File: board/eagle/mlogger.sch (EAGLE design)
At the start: 40 parts, among them J1 MICROSD-9P, SW1 SS-12D00G3, SW2 TVAF06-A020B-R, SW3 TVAF06-A020B-R

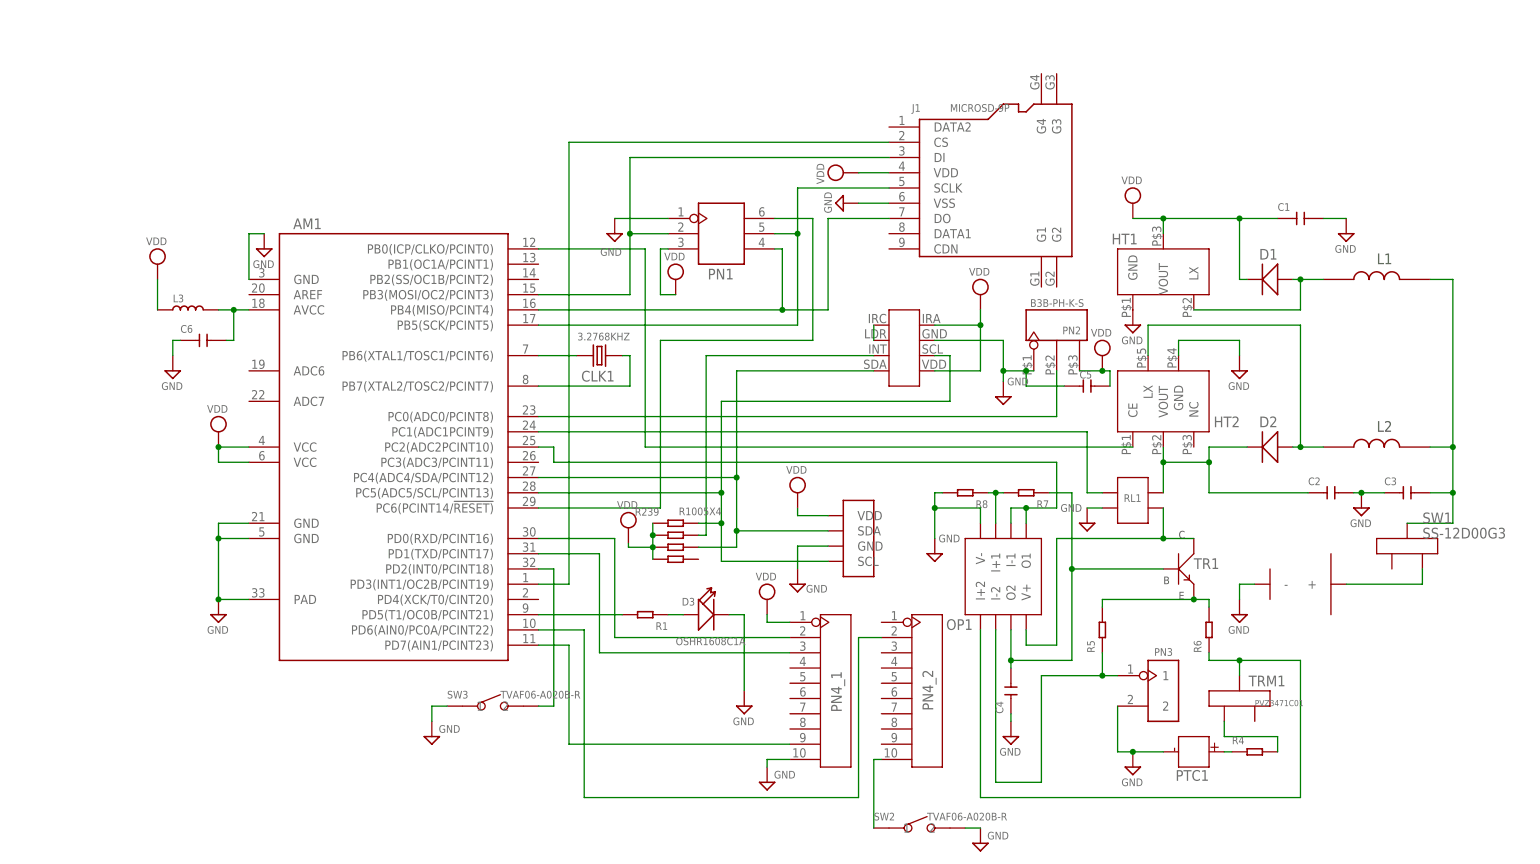
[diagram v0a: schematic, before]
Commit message: AVR32DB32を使ったVersion3.0の開発開始。
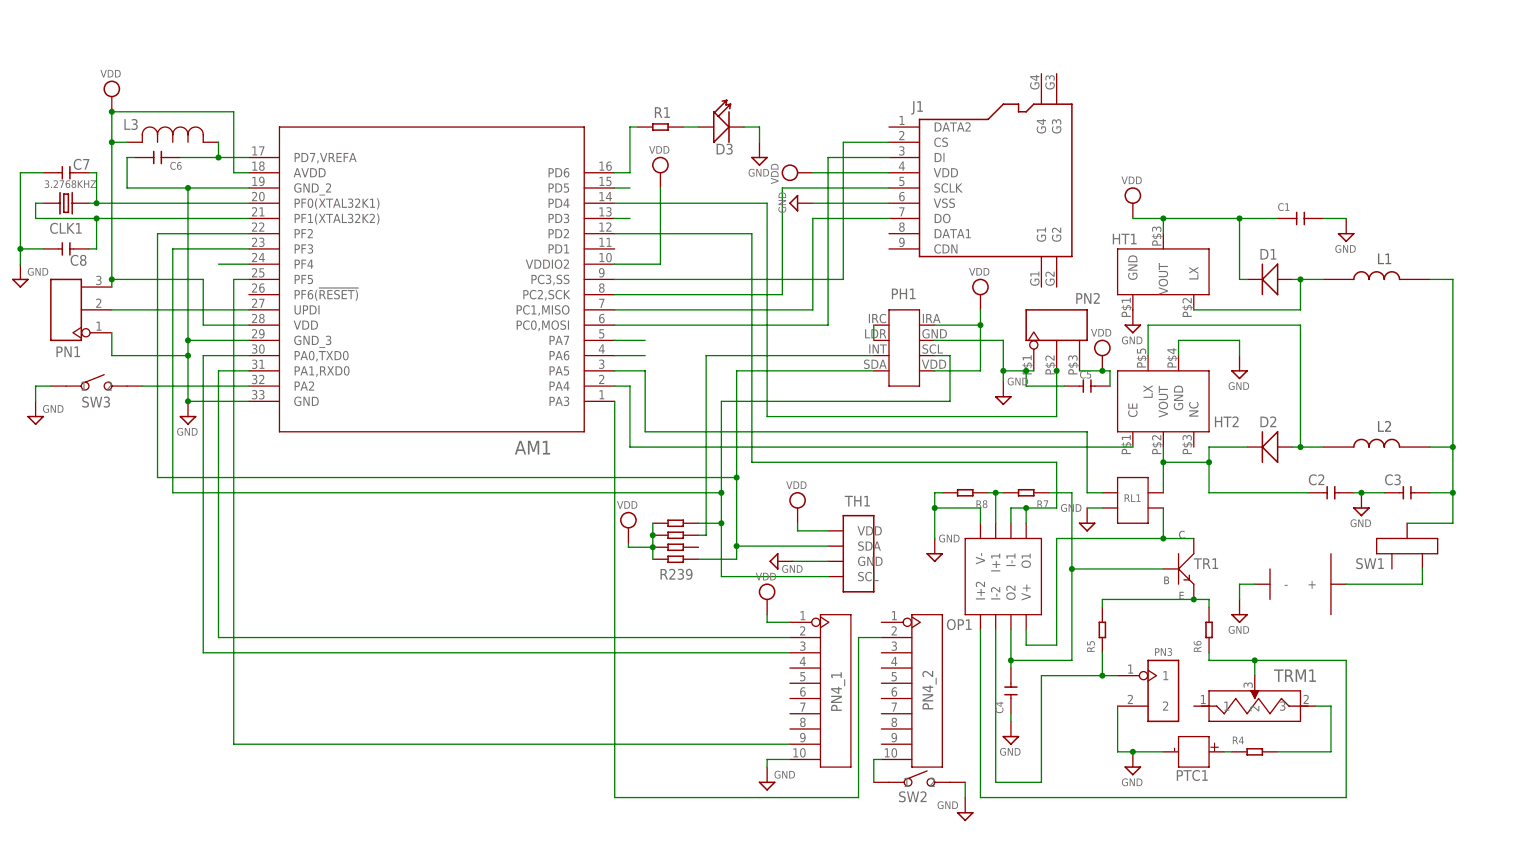
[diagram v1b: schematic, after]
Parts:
- added C7, C8: (no value), MyParts:MURATA_0603
- AM1: value ATMEGA328P-MU-QFN32 -> AVR64DB32-I/RXBVQFN32_RXB_MCH; device Seeed-IC:MCU-ATMEGA328P-MU(QFN32) -> MyParts:AVR64DB32-I/RXBVQFN32_RXB_MCH
- L3: value (none) -> LBR2012T100KIND_TAIYO_LBR2012_TAY; device MyParts:DFE322512F-100M -> MyParts:LBR2012T100KIND_TAIYO_LBR2012_TAY
- PN1: value 2x3p-2.54 -> 3p-2.54; device MyParts:DIP-BLACK-MALE-HEADER(2X3P-2.54）-2.54 -> MyParts:DIP-BLACK-MALE-HEADER-VERT(3P-2.54)
- TRM1: value PVZ3471C01 -> TC33X-1-103EIND_1-103E-L; device MyParts:PVZ3471C01 -> MyParts:TC33X-1-103EIND_1-103E-L
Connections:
- removed net AVCC: AM1.AVCC, C6.2, L3.2
- removed net N$17: R4.2, TRM1.P3
- removed net N$33: AM1.PD3(INT1/OC2B/PCINT19), J1.CS
- removed net XTAL1: AM1.PB6(XTAL1/TOSC1/PCINT6), CLK1.2
- removed net XTAL2: AM1.PB7(XTAL2/TOSC2/PCINT7), CLK1.1
- new net N$11: AM1.PD5
- new net N$12: AM1.PA7
- new net N$13: AM1.PA6
- new net N$2: AM1.PF0(XTAL32K1), C7.1, CLK1.1
- new net N$6: AM1.PF1(XTAL32K2), C8.1, CLK1.2
- new net N$7: AM1.UPDI, PN1.P$2
- new net N$8: AM1.PD3
- new net N$9: AM1.PF4
- new net SS: AM1.PC3,SS, J1.CS
- new net VREFA: AM1.PD7,VREFA, C6.2, L3.1
- net ADC0: now also AM1.PD4; no longer AM1.PC0(ADC0/PCINT8)
- net ADC2: now also AM1.PD2; no longer AM1.PC2(ADC2PCINT10)
- net CTS: now also AM1.PA3; no longer AM1.PD6(AIN0/PC0A/PCINT22)
- net GND: now also AM1.GND_2, AM1.GND_3, C7.2, C8.2, PN1.P$1; no longer AM1.GND@1, AM1.GND@2, AM1.PAD, PN1.1
- net MISO: now also AM1.PC1,MISO; no longer AM1.PB4(MISO/PCINT4), PN1.4
- net MOSI: now also AM1.PC0,MOSI; no longer AM1.PB3(MOSI/OC2/PCINT3), PN1.2
- net N$1: now also R4.2, TRM1.3; no longer AM1.PD5(T1/OC0B/PCINT21), R1.2
- net N$23: now also AM1.PA4; no longer AM1.PB0(ICP/CLKO/PCINT0)
- net N$24: now also AM1.PA5; no longer AM1.PC1(ADC1PCINT9)
- net N$4: now also AM1.PD6, R1.2; no longer AM1.PC6(PCINT14/!RESET), PN1.6
- net N$5: now also AM1.PA2; no longer AM1.PD2(INT0/PCINT18)
- net P$3: now also TRM1.2; no longer TRM1.P2
- net RXD: now also AM1.PA1,RXD0; no longer AM1.PD0(RXD/PCINT16)
- net SCK: now also AM1.PC2,SCK; no longer AM1.PB5(SCK/PCINT5), PN1.5
- net SCL: now also AM1.PF3; no longer AM1.PC5(ADC5/SCL/PCINT13)
- net SDA: now also AM1.PF2, R239.8; no longer AM1.PC4(ADC4/SDA/PCINT12), R239.6
- net SLP: now also AM1.PF5; no longer AM1.PD7(AIN1/PCINT23)
- net TXD: now also AM1.PA0,TXD0; no longer AM1.PD1(TXD/PCINT17)
- net VDD: now also AM1.AVDD, AM1.VDD, AM1.VDDIO2, L3.2, PN1.P$3; no longer AM1.VCC@1, AM1.VCC@2, L3.1, PN1.3
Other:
- note added: "PH1"
- note added: "TH1"
- moved on the sheet: C6, CLK1, D3, R1, SW2, SW3

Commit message: 基板形状微修正
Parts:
- renumbered BBOX to BB1, PN4_1 to PN4_1(XB1), PN4_2 to PN4_2(XB1)
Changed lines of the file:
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@@
 <part name="SUPPLY18" library="supply2" library_urn="urn:adsk.eagle:library:372" deviceset="GND" device=""/>
 <part name="SUPPLY23" library="supply2" library_urn="urn:adsk.eagle:library:372" deviceset="GND" device=""/>
-<part name="PN4_1" library="OPL_Connector" library_urn="urn:adsk.eagle:library:8004395" deviceset="DIP-BLACK-FEMALE-HEADER-VERT(10P-2.0)" device="" package3d_urn="urn:adsk.eagle:package:8004550/1" value="10p-2.0"/>
+<part name="PN4_1(XB1)" library="OPL_Connector" library_urn="urn:adsk.eagle:library:8004395" deviceset="DIP-BLACK-FEMALE-HEADER-VERT(10P-2.0)" device="" package3d_urn="urn:adsk.eagle:package:8004550/1" value="10p-2.0"/>
 <part name="SUPPLY7" library="supply2" library_urn="urn:adsk.eagle:library:372" deviceset="VDD" device=""/>
-<part name="PN4_2" library="OPL_Connector" library_urn="urn:adsk.eagle:library:8004395" deviceset="DIP-BLACK-FEMALE-HEADER-VERT(10P-2.0)" device="" package3d_urn="urn:adsk.eagle:package:8004550/1" value="10p-2.0"/>
+<part name="PN4_2(XB1)" library="OPL_Connector" library_urn="urn:adsk.eagle:library:8004395" deviceset="DIP-BLACK-FEMALE-HEADER-VERT(10P-2.0)" device="" package3d_urn="urn:adsk.eagle:package:8004550/1" value="10p-2.0"/>
 <part name="SUPPLY8" library="supply2" library_urn="urn:adsk.eagle:library:372" deviceset="GND" device=""/>
 <part name="SUPPLY12" library="supply2" library_urn="urn:adsk.eagle:library:372" deviceset="GND" device=""/>
@@
 <part name="SUPPLY11" library="supply2" library_urn="urn:adsk.eagle:library:372" deviceset="GND" device=""/>
 <part name="PTC1" library="MyParts" deviceset="TFPT1206" device=""/>
-<part name="BBOX" library="MyParts" deviceset="BH321" device=""/>
+<part name="BB1" library="MyParts" deviceset="BH321" device=""/>
 <part name="SUPPLY14" library="supply2" library_urn="urn:adsk.eagle:library:372" deviceset="GND" device=""/>
 <part name="SUPPLY21" library="supply2" library_urn="urn:adsk.eagle:library:372" deviceset="VDD" device=""/>
@@
 <attribute name="VALUE" x="-18.415" y="80.645" size="1.27" layer="96"/>
 </instance>
-<instance part="PN4_1" gate="G$1" x="-5.08" y="-5.08" smashed="yes">
+<instance part="PN4_1(XB1)" gate="G$1" x="-5.08" y="-5.08" smashed="yes">
 <attribute name="NAME" x="-2.794" y="-8.636" size="1.778" layer="95" ratio="10" rot="R90"/>
 </instance>
@@
 <attribute name="VALUE" x="-17.145" y="13.335" size="1.27" layer="96"/>
 </instance>
-<instance part="PN4_2" gate="G$1" x="10.16" y="-5.08" smashed="yes">
+<instance part="PN4_2(XB1)" gate="G$1" x="10.16" y="-5.08" smashed="yes">
 <attribute name="NAME" x="12.446" y="-8.382" size="1.778" layer="95" ratio="10" rot="R90"/>
 </instance>
@@
 <attribute name="NAME" x="52.832" y="-20.066" size="1.778" layer="95"/>
 </instance>
-<instance part="BBOX" gate="G$1" x="68.58" y="10.16" smashed="yes"/>
+<instance part="BB1" gate="G$1" x="68.58" y="10.16" smashed="yes"/>
 <instance part="SUPPLY14" gate="GND" x="25.4" y="-12.7" smashed="yes">
 <attribute name="VALUE" x="23.495" y="-15.875" size="1.27" layer="96"/>
@@
 </segment>
 <segment>
-<pinref part="PN4_1" gate="G$1" pin="10"/>
+<pinref part="PN4_1(XB1)" gate="G$1" pin="10"/>
 <pinref part="SUPPLY12" gate="GND" pin="GND"/>
 <wire x1="-11.43" y1="-16.51" x2="-15.24" y2="-16.51" width="0.1524" layer="91"/>
@@
 <pinref part="SUPPLY16" gate="GND" pin="GND"/>
 <wire x1="63.5" y1="10.16" x2="63.5" y2="12.7" width="0.1524" layer="91"/>
-<pinref part="BBOX" gate="G$1" pin="-"/>
+<pinref part="BB1" gate="G$1" pin="-"/>
 <wire x1="66.04" y1="12.7" x2="63.5" y2="12.7" width="0.1524" layer="91"/>
 </segment>
@@
 <net name="VDD" class="2">
 <segment>
-<pinref part="PN4_1" gate="G$1" pin="1"/>
+<pinref part="PN4_1(XB1)" gate="G$1" pin="1"/>
 <pinref part="SUPPLY7" gate="G$1" pin="VDD"/>
 <wire x1="-11.43" y1="6.35" x2="-15.24" y2="6.35" width="0.1524" layer="91"/>
@@
 <net name="RXD" class="0">
 <segment>
-<pinref part="PN4_1" gate="G$1" pin="2"/>
+<pinref part="PN4_1(XB1)" gate="G$1" pin="2"/>
 <wire x1="-106.68" y1="3.81" x2="-11.43" y2="3.81" width="0.1524" layer="91"/>
 <pinref part="AM1" gate="A" pin="PA1,RXD0"/>
@@
 <net name="TXD" class="0">
 <segment>
-<pinref part="PN4_1" gate="G$1" pin="3"/>
+<pinref part="PN4_1(XB1)" gate="G$1" pin="3"/>
 <wire x1="-109.22" y1="1.27" x2="-11.43" y2="1.27" width="0.1524" layer="91"/>
 <wire x1="-109.22" y1="1.27" x2="-109.22" y2="50.8" width="0.1524" layer="91"/>
@@
 <net name="SLP" class="0">
 <segment>
-<pinref part="PN4_1" gate="G$1" pin="9"/>
+<pinref part="PN4_1(XB1)" gate="G$1" pin="9"/>
 <wire x1="-104.14" y1="63.5" x2="-104.14" y2="-13.97" width="0.1524" layer="91"/>
 <wire x1="-104.14" y1="-13.97" x2="-11.43" y2="-13.97" width="0.1524" layer="91"/>
@@
 <net name="CTS" class="0">
 <segment>
-<pinref part="PN4_2" gate="G$1" pin="2"/>
+<pinref part="PN4_2(XB1)" gate="G$1" pin="2"/>
 <wire x1="3.81" y1="3.81" x2="0" y2="3.81" width="0.1524" layer="91"/>
 <wire x1="0" y1="3.81" x2="0" y2="-22.86" width="0.1524" layer="91"/>
@@
 <net name="N$3" class="0">
 <segment>
-<pinref part="PN4_2" gate="G$1" pin="10"/>
+<pinref part="PN4_2(XB1)" gate="G$1" pin="10"/>
 <wire x1="3.81" y1="-16.51" x2="2.54" y2="-16.51" width="0.1524" layer="91"/>
 <wire x1="2.54" y1="-16.51" x2="2.54" y2="-20.32" width="0.1524" layer="91"/>
@@
 <net name="VBT" class="0">
 <segment>
-<pinref part="BBOX" gate="G$1" pin="+"/>
+<pinref part="BB1" gate="G$1" pin="+"/>
 <pinref part="SW1" gate="G$1" pin="P1"/>
 <wire x1="81.28" y1="12.7" x2="93.98" y2="12.7" width="0.1524" layer="91"/>
